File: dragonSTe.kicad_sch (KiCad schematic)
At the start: 0 parts

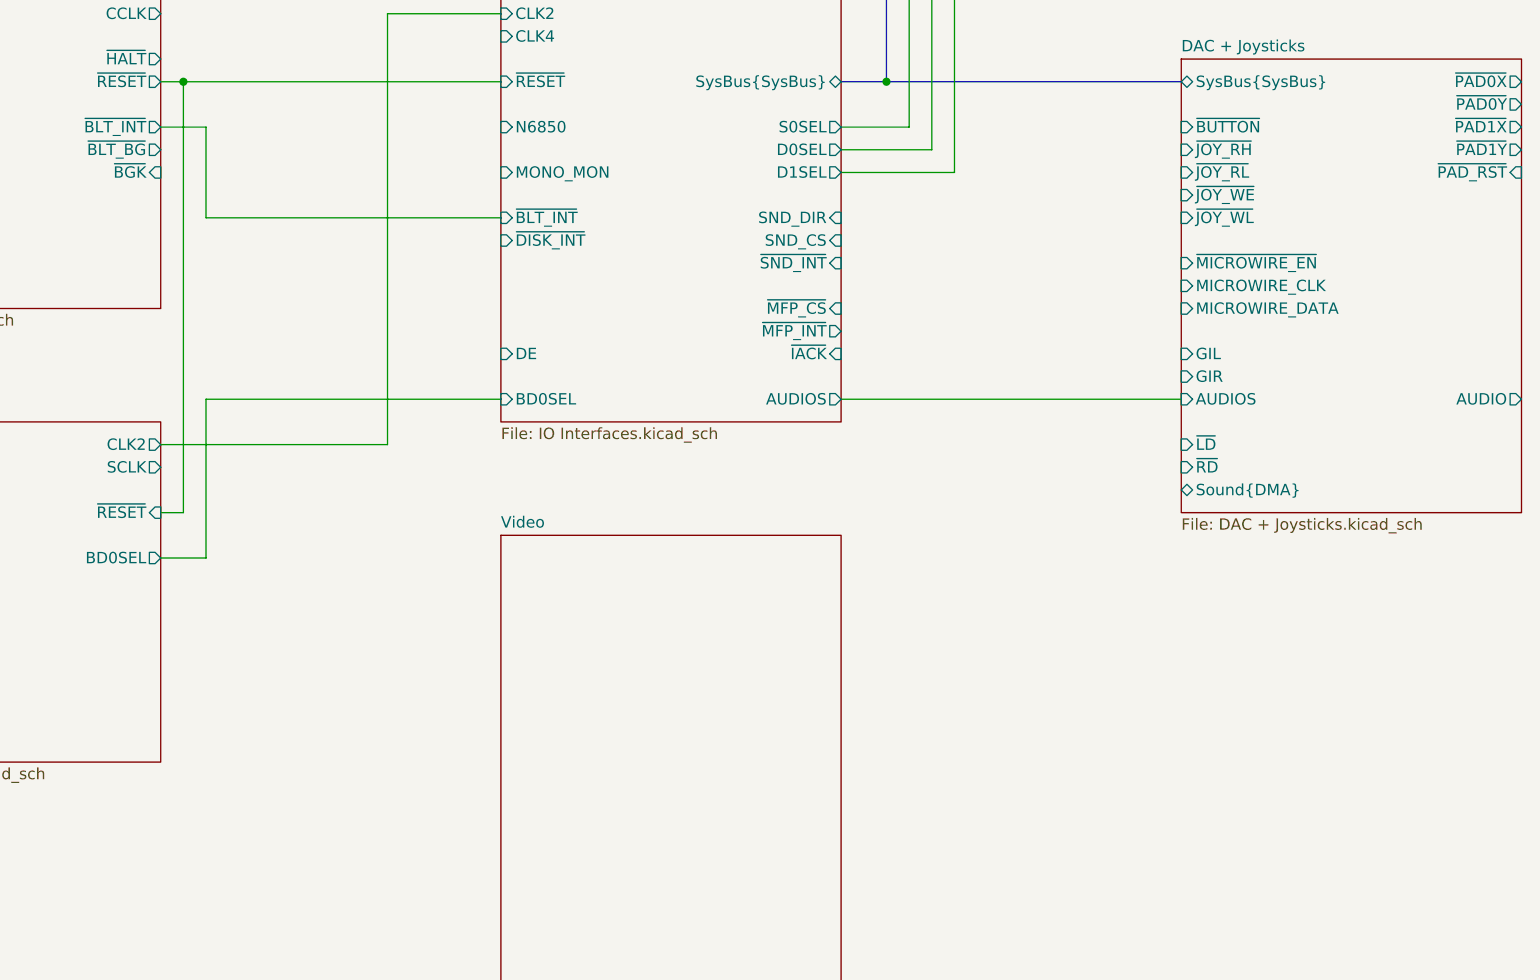
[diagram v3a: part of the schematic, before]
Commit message: motherboard: Added SHIFTER to the schematic and tidied up a pile
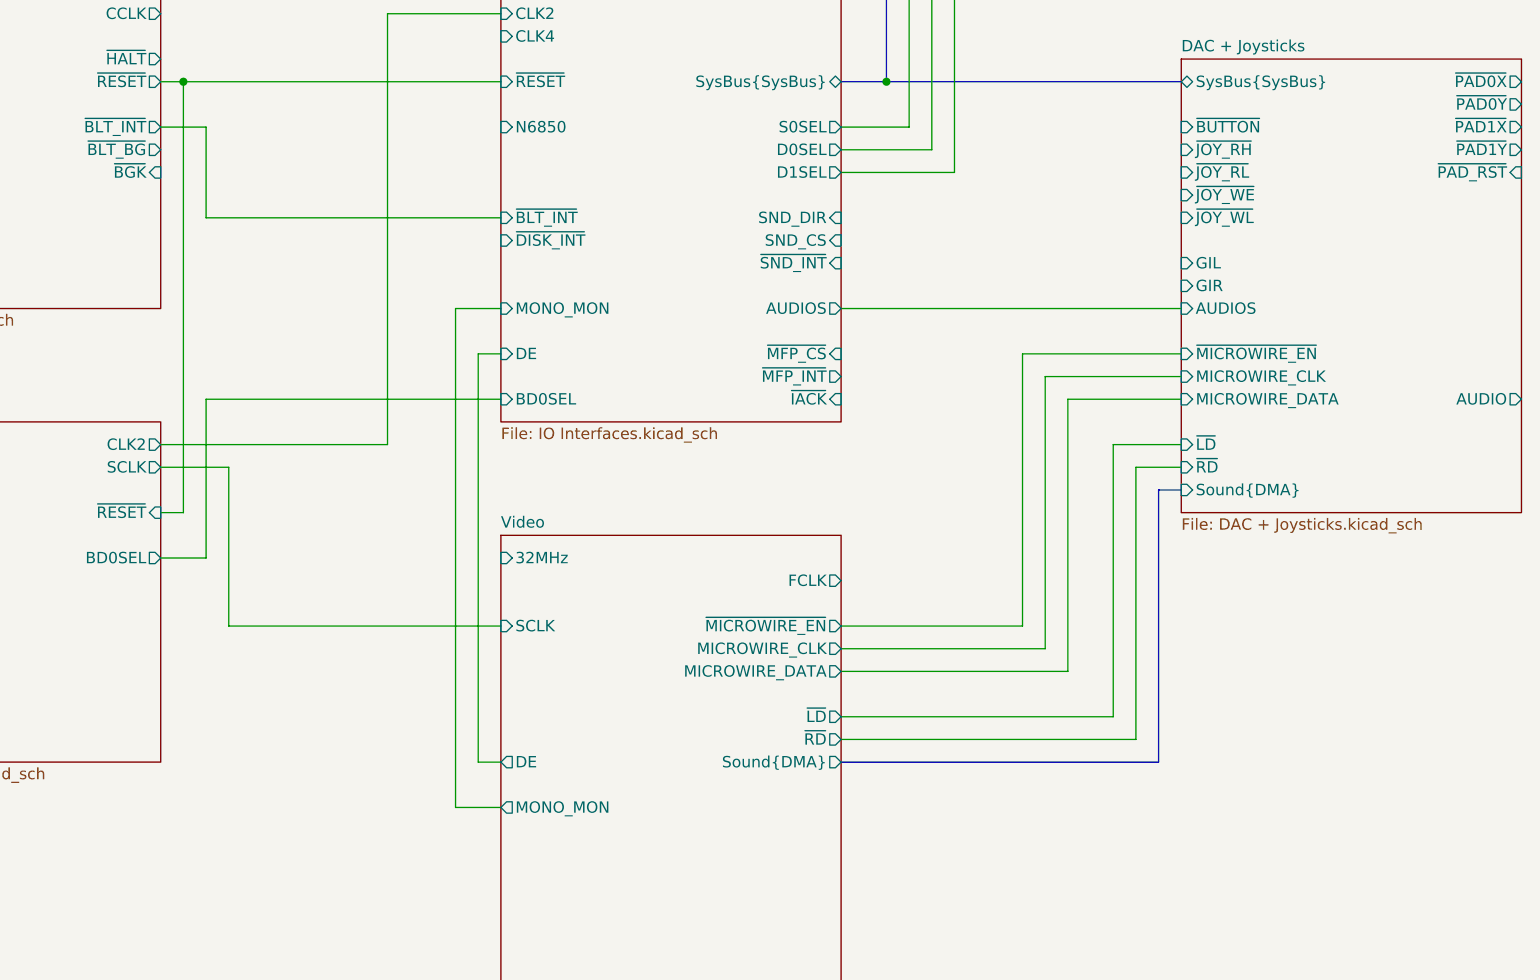
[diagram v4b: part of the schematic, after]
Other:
- sheet Video ports: added 32MHz, DE, FCLK, MICROWIRE_CLK, MICROWIRE_DATA, MONO_MON, SCLK, Sound{DMA}, ~{LD}, ~{MICROWIRE_EN}, ~{RD}; removed none

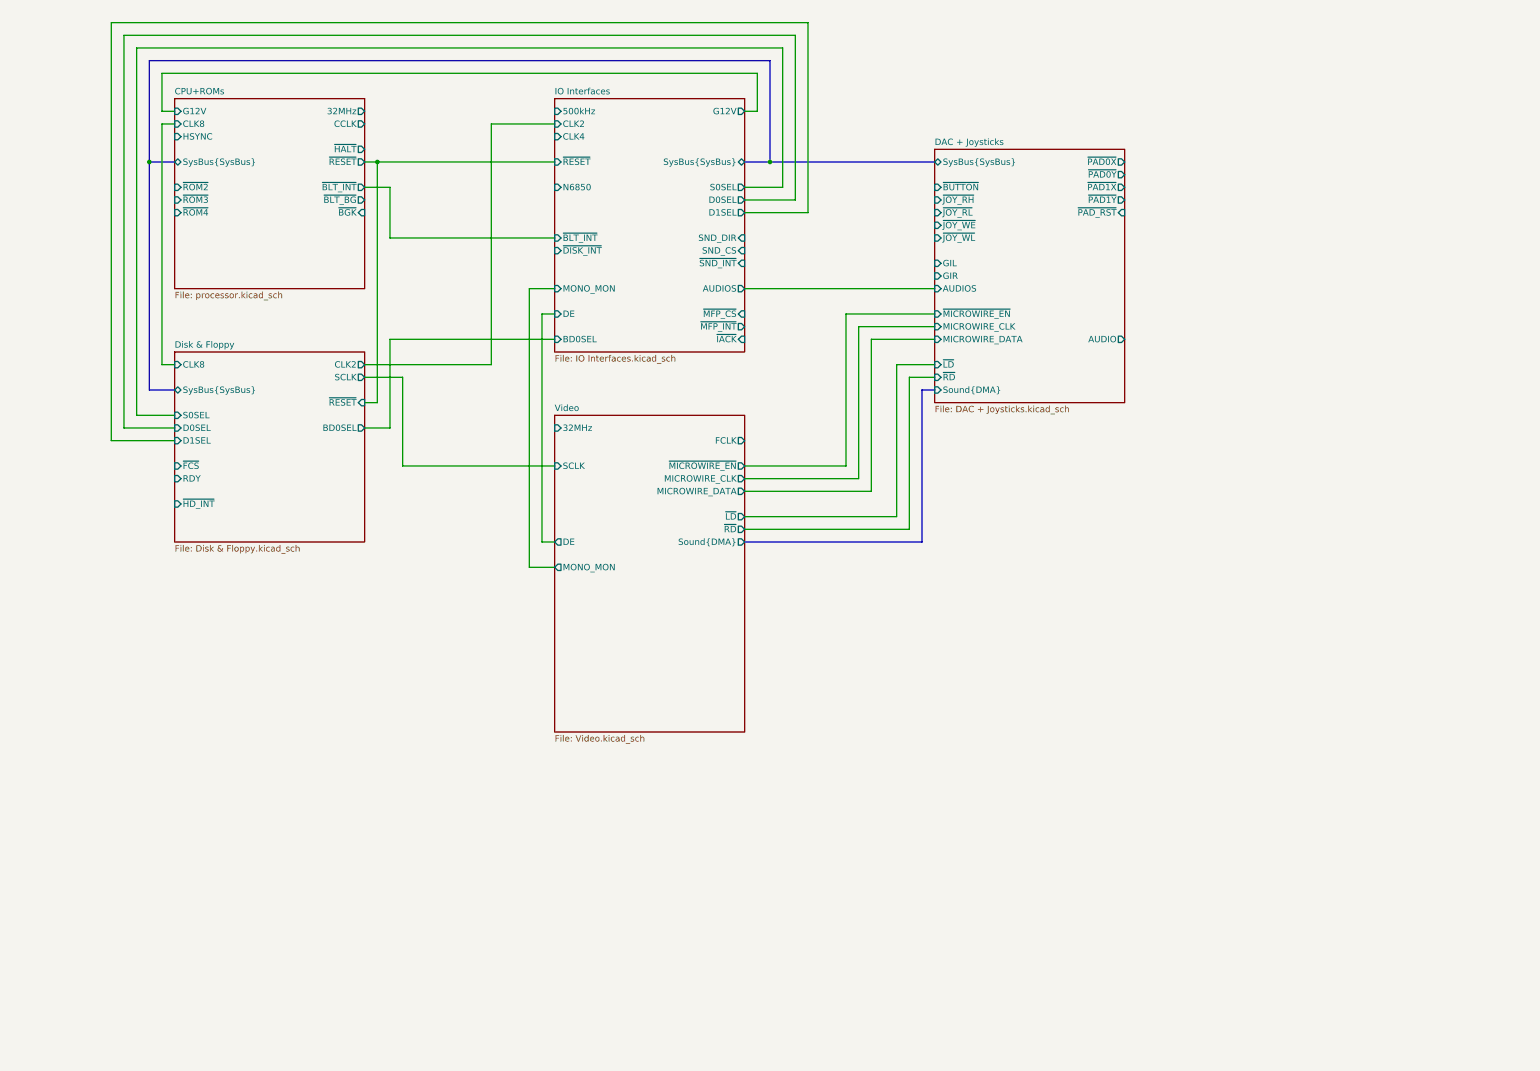
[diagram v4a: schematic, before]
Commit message: motherboard: Worked on fleshing out more of the top-level schematic, filling in more of the connections that need to be made between blocks
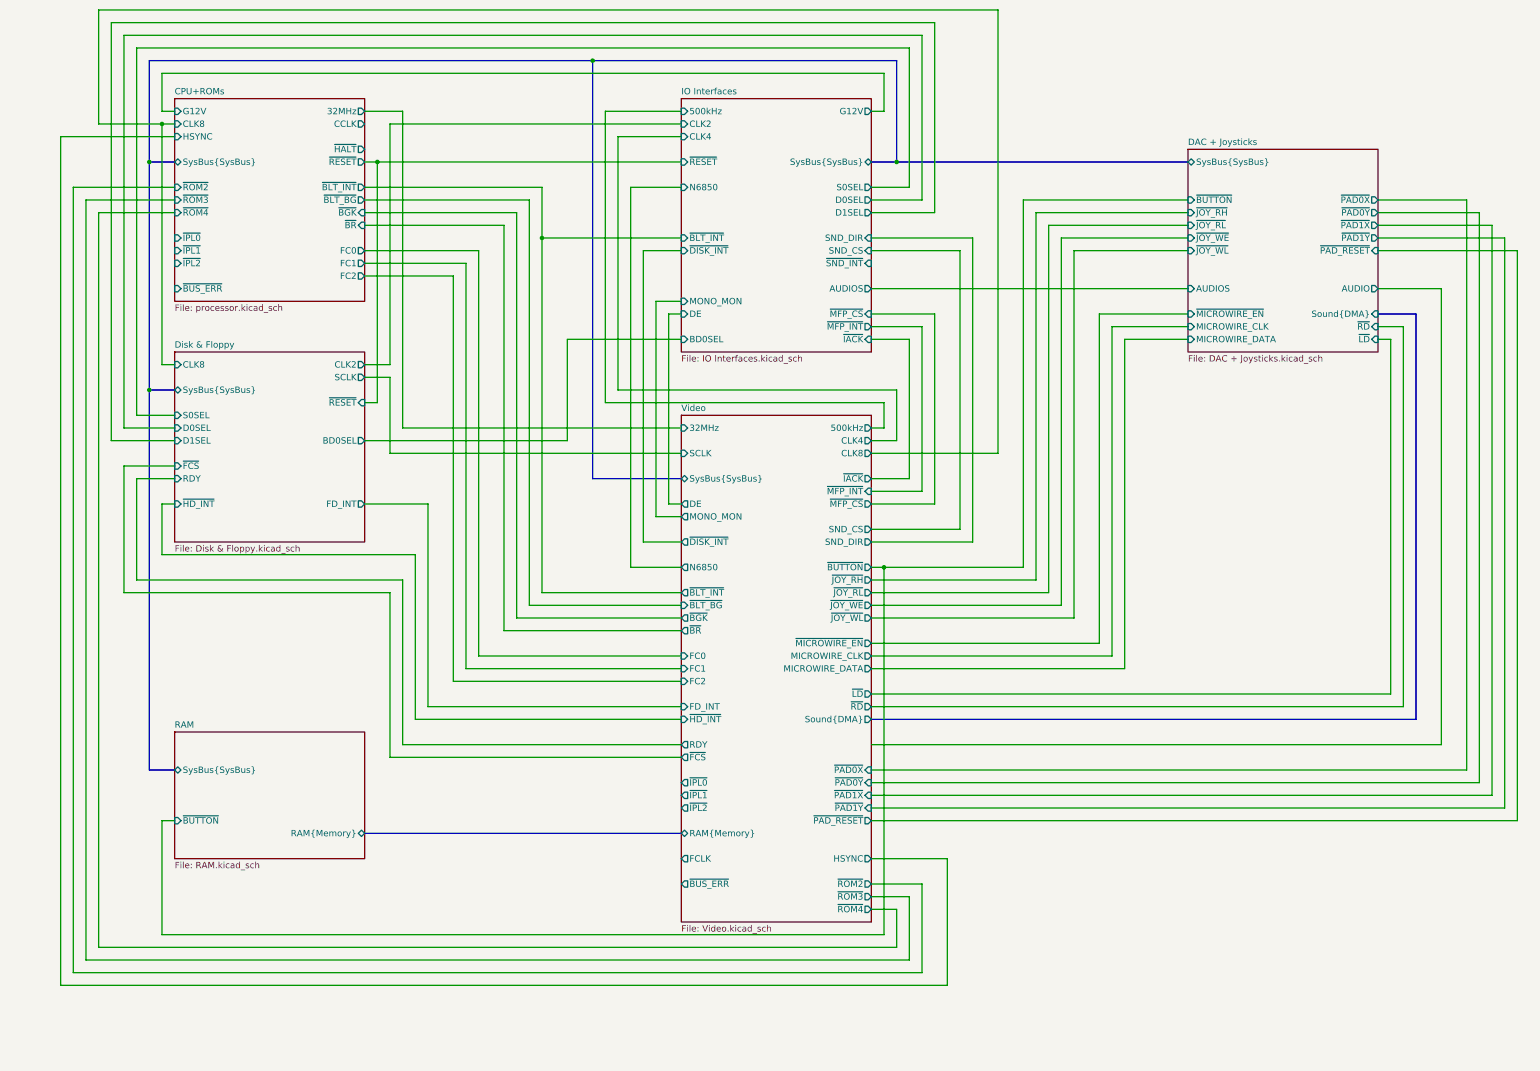
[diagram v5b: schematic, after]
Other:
- added sheet RAM (RAM.kicad_sch)
- sheet CPU+ROMs ports: added FC0, FC1, FC2, ~{BR}, ~{BUS_ERR}, ~{IPL0}, ~{IPL1}, ~{IPL2}; removed none
- sheet DAC + Joysticks ports: added ~{PAD_RESET}; removed GIL, GIR, ~{PAD_RST}
- sheet Disk & Floppy ports: added FD_INT; removed none
- sheet Video ports: added 500kHz, CLK4, CLK8, FC0, FC1, FC2, FD_INT, HSYNC, N6850, RAM{Memory}, RDY, SND_CS, SND_DIR, SysBus{SysBus}, ~{BGK}, ~{BLT_BG}, ~{BLT_INT}, ~{BR}, ~{BUS_ERR}, ~{BUTTON}, ~{DISK_INT}, ~{FCS}, ~{HD_INT}, ~{IACK}, ~{IPL0}, ~{IPL1}, ~{IPL2}, ~{JOY_RH}, ~{JOY_RL}, ~{JOY_WE}, ~{JOY_WL}, ~{MFP_CS}, ~{MFP_INT}, ~{PAD0X}, ~{PAD0Y}, ~{PAD1X}, ~{PAD1Y}, ~{PAD_RESET}, ~{ROM2}, ~{ROM3}, ~{ROM4}; removed none

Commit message: motherboard: More signal routing, and starting in on the BoM
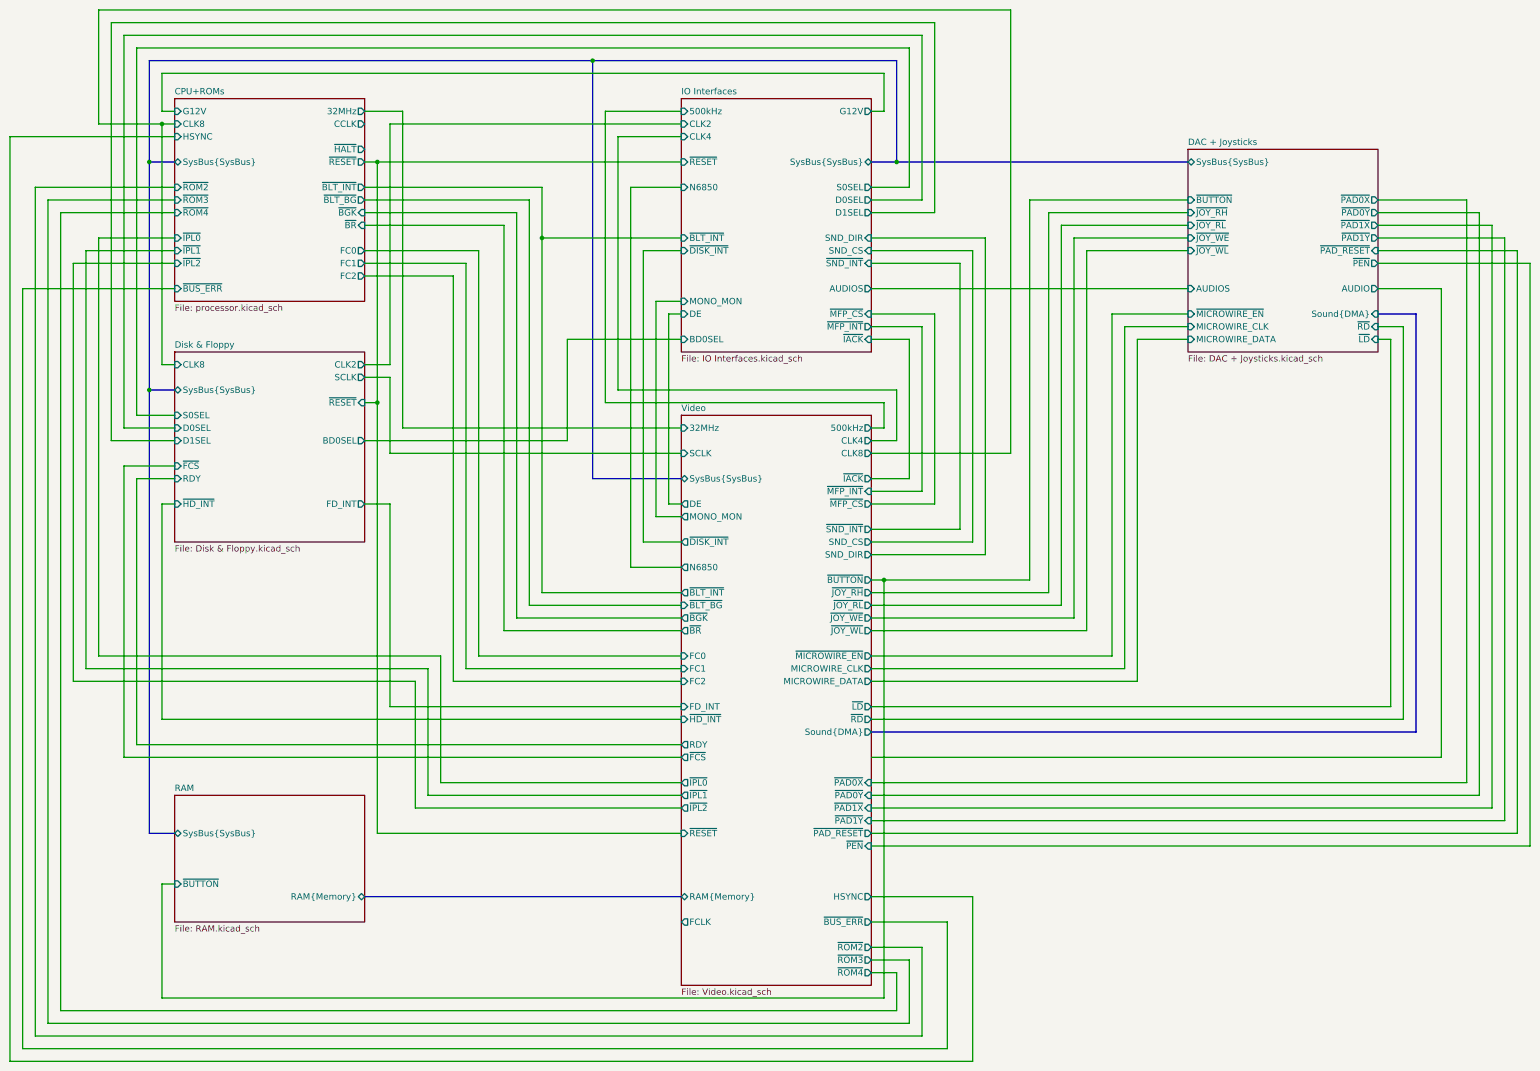
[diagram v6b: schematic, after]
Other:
- sheet DAC + Joysticks ports: added ~{PEN}; removed none
- sheet Video ports: added ~{PEN}, ~{RESET}, ~{SND_INT}; removed none

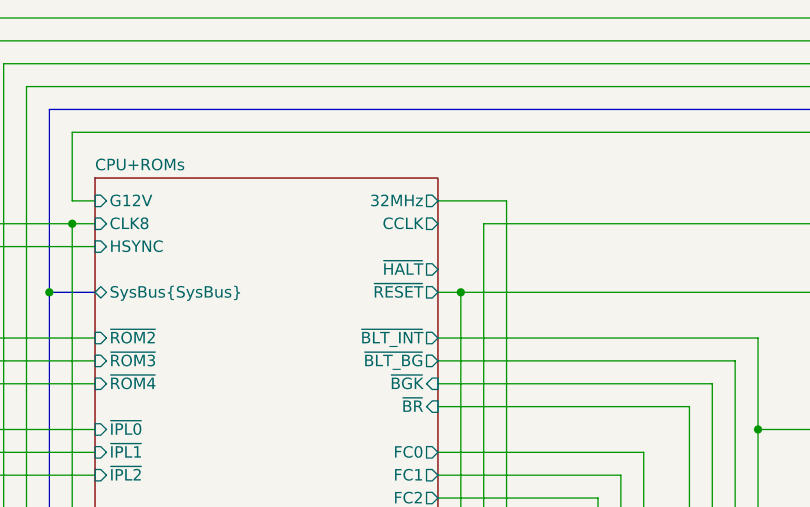
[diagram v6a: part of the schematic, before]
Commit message: motherboard: Cleaned up the clock tree implementation, specifying and fixing down how to do the 32MHz clock source
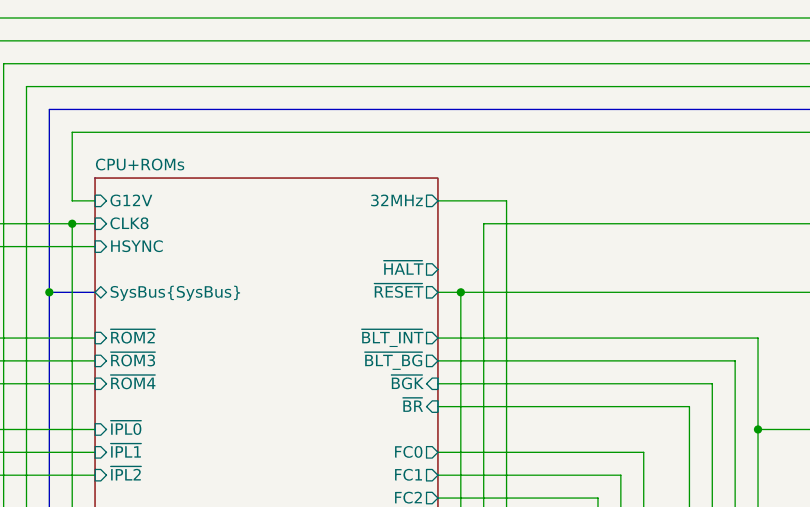
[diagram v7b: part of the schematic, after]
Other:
- sheet CPU+ROMs ports: added none; removed CCLK
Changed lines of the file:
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@@
-			)
-		)
-		(pin "CCLK" output
-			(at 88.9 55.88 0)
-			(effects
-				(font
-					(size 1.27 1.27)
-				)
-				(justify right)
 			)
 		)
